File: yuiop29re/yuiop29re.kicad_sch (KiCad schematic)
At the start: 123 parts, among them J1 USB_C_Receptacle_USB2.0_16P, J2 SSD1306 OLED, J3 AudioJack4, J4 UART0, J5 SWD, Q1 BSS138, U1 RP2040_breakout

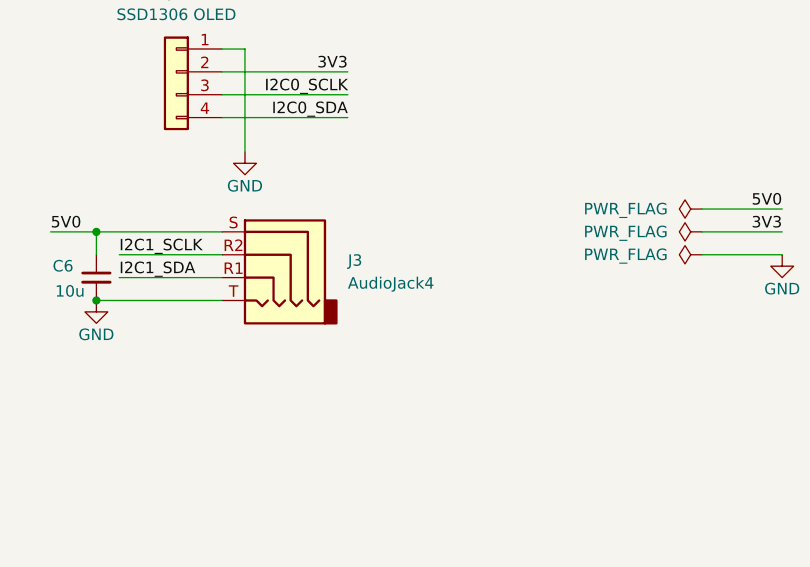
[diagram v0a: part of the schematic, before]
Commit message: yuiop29re: improve TRRS jack
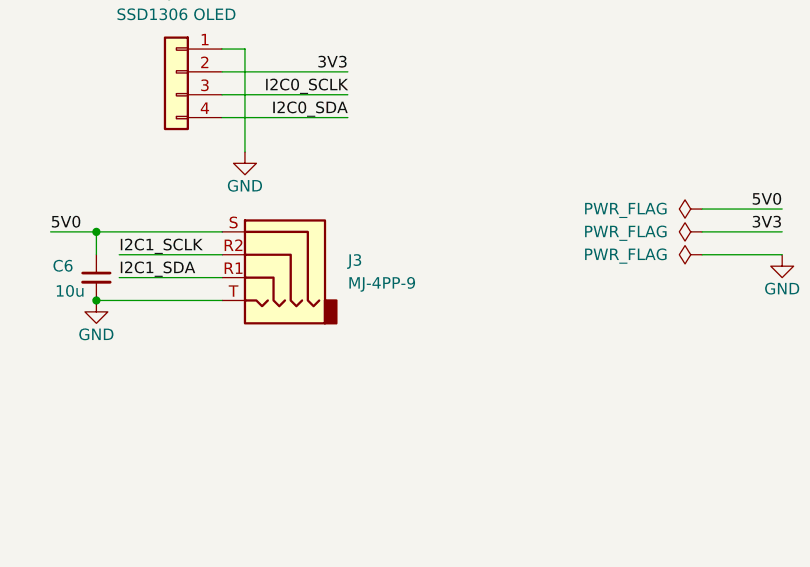
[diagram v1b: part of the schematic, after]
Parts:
- J3: value AudioJack4 -> MJ-4PP-9; footprint Connector_Audio:Jack_3.5mm_PJ320E_Horizontal -> yuiop:MJ-4PP-9
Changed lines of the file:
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@@
 			)
 		)
-		(property "Value" "AudioJack4"
+		(property "Value" "MJ-4PP-9"
 			(at 199.39 150.4949 0)
 			(effects
@@
 			)
 		)
-		(property "Footprint" "Connector_Audio:Jack_3.5mm_PJ320E_Horizontal"
+		(property "Footprint" "yuiop:MJ-4PP-9"
 			(at 190.5 147.32 0)
 			(effects
@@
 			)
 		)
-		(property "Datasheet" "~"
+		(property "Datasheet" "https://akizukidenshi.com/catalog/g/g106070/"
 			(at 190.5 147.32 0)
 			(effects

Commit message: update TRRS jack footprint to new version
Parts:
- J3: footprint yuiop:MJ-4PP-9 -> yuiop:MJ-4PP-9_2021
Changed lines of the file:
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@@
 			)
 		)
-		(property "Footprint" "yuiop:MJ-4PP-9"
+		(property "Footprint" "yuiop:MJ-4PP-9_2021"
 			(at 190.5 147.32 0)
 			(effects

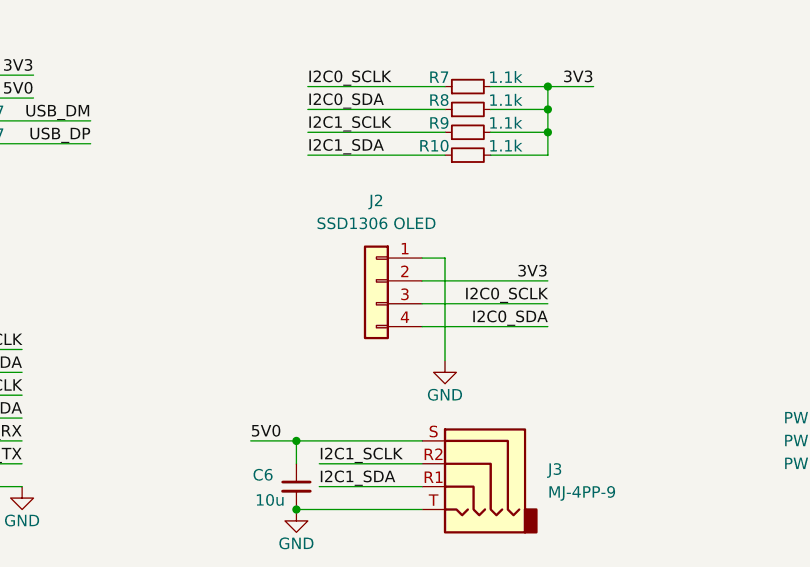
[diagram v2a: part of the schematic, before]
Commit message: fix OLED footprint
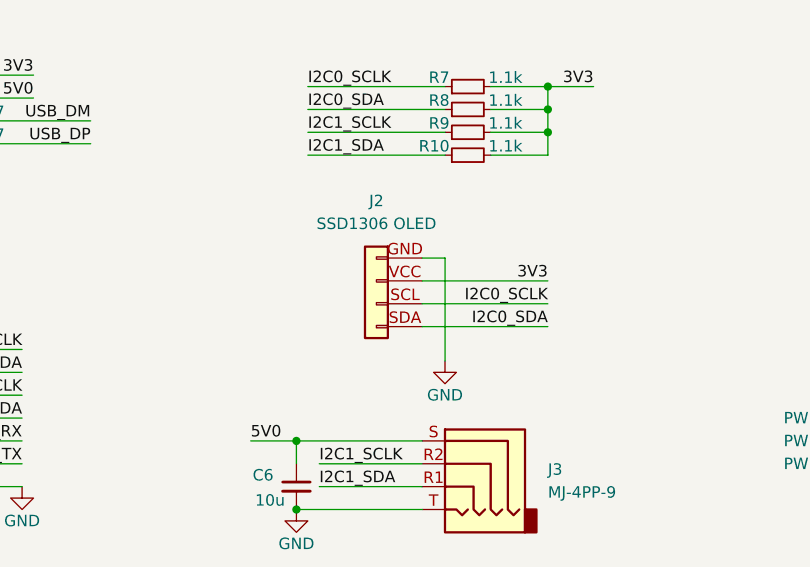
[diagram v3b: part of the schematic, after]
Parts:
- J2: footprint Connector_PinHeader_1.00mm:PinHeader_1x04_P1.00mm_Vertical -> yuiop:OLED_128x32
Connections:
- net 3V3: now also J2.VCC (Pin_2); no longer J2.2 (Pin_2)
- net GND: now also J2.GND (Pin_1); no longer J2.1 (Pin_1)
- net I2C0_SCLK: now also J2.SCL (Pin_3); no longer J2.3 (Pin_3)
- net I2C0_SDA: now also J2.SDA (Pin_4); no longer J2.4 (Pin_4)
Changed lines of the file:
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@@
 			)
 		)
-		(property "Footprint" "Connector_PinHeader_1.00mm:PinHeader_1x04_P1.00mm_Vertical"
+		(property "Footprint" "yuiop:OLED_128x32"
 			(at 180.34 127 0)
 			(effects
@@
 			)
 		)
-		(pin "1"
+		(pin "GND"
 		)
-		(pin "4"
+		(pin "SCL"
 		)
-		(pin "3"
+		(pin "SDA"
 		)
-		(pin "2"
+		(pin "VCC"
 		)
 		(instances

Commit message: yuiop29re: wiring completed
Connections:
- net USB_DM: now also R4.2; no longer R3.2
- net USB_DP: now also R3.2; no longer R4.2
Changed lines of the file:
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@@
 		)
 	)
-	(label "USB_DM"
+	(label "USB_DP"
 		(at 148.59 109.22 180)
 		(fields_autoplaced yes)
@@
 		)
 	)
-	(label "USB_DP"
+	(label "USB_DM"
 		(at 148.59 111.76 180)
 		(fields_autoplaced yes)
